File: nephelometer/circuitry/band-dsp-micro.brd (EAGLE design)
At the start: 88 x 54 mm, 41 parts, among them IC8 7805TV, J1 J5MM, T1 2N2222, T2 2N2222, U4 MotA

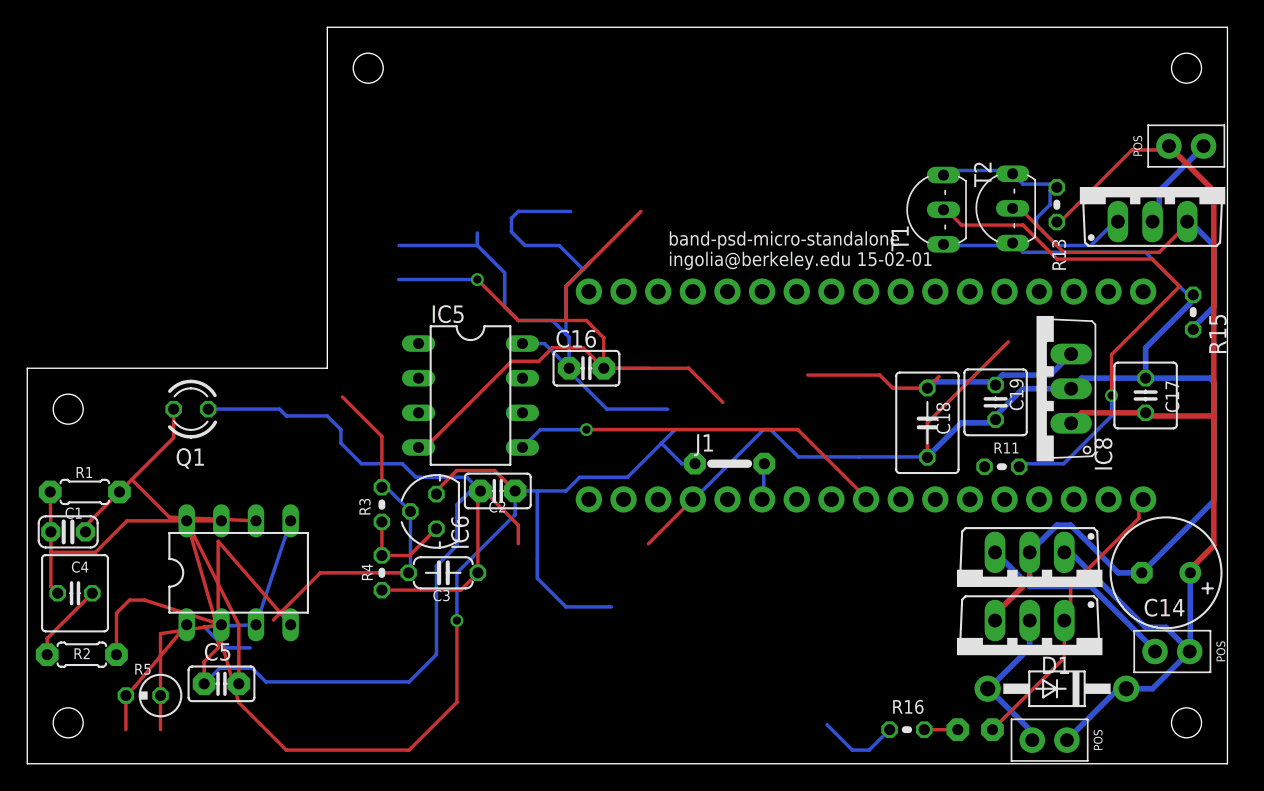
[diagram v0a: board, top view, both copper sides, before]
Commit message: Finalized minimal turbidostat circuit with Arduino Micro control
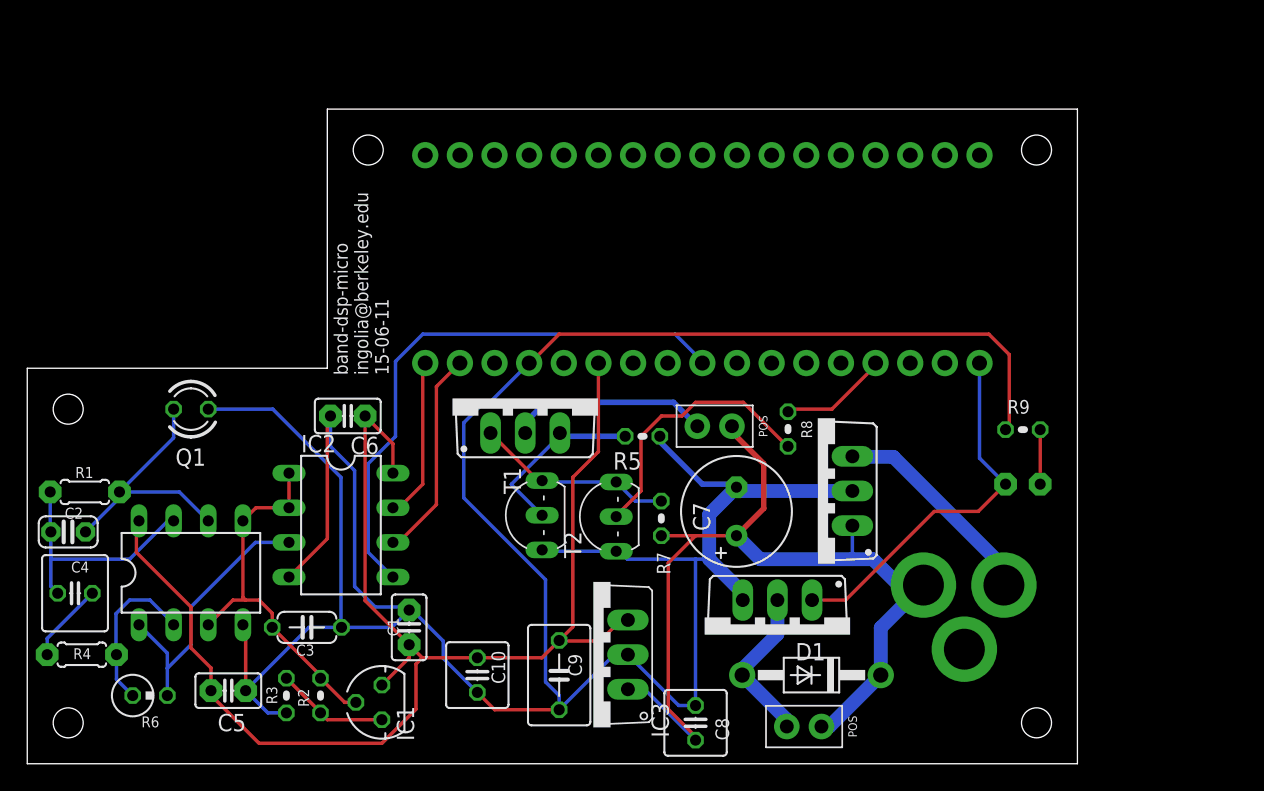
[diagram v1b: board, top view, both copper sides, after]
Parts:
- removed C14: 220µF, adafruit:E3,5-8
- removed C16: 100n, adafruit:C025-025X050
- removed C17, C19: 0.33µ, adafruit:C025-050X050
- removed C18: 22µ, adafruit:C050-045X075
- removed IC5: (no value), ingolia:DIL08
- removed IC6: (no value), v-reg:317L
- removed IC8: 7805TV, linear:TO220V
- removed R11, R13: 4K7, adafruit:0204V
- removed R15: 6.2R, adafruit:0204V
- removed R16: 330, adafruit:0204V
- removed U4: MotA, ingolia:1X02_SCREW
- added C10, C8: 0.33µ, adafruit:C025-050X050
- added C6: 100n, adafruit:C025-025X050
- added C7: 220µF, adafruit:E3,5-8
- added C9: 22µ, adafruit:C050-045X075
- added IC2, U1: (no value), ingolia:DIL08
- added IC3: 7805TV, linear:TO220V
- added R6: 2M0, adafruit:0309V
- added R7, R8: 4K7, adafruit:0204V
- added R9: 330, adafruit:0204V
- C1: value 2.2nF -> 100nF; device adafruit:C025-024X044 -> adafruit:C025-025X050
- C2: value 100nF -> 2.2nF; device adafruit:C025-025X050 -> adafruit:C025-024X044
- IC1: device ingolia:DIL08 -> v-reg:317L
- J1: value J5MM -> 2.1MMJACKTHM; device jumper:05 -> adafruit:PJ-102A
- R2: value 1K0 -> 120; device adafruit:0204/5 -> adafruit:0204V
- R4: value 120 -> 10K; device adafruit:0204V -> adafruit:0204/5
- R5: value 330K -> 10R; device adafruit:0309V -> adafruit:0204V
- U2: value (none) -> MotA
- moved Q2 48.5 mm to (36.5, 30.2)
- moved R5 41.3 mm to (45.1, 30.0)
- moved T1 37.0 mm to (36.5, 24.2)
- moved T2 36.8 mm to (41.9, 24.1)
- moved JP1 34.6 mm to (52.9, 32.0), turned to 180 degrees
- moved C2 31.6 mm to (3.00, 23.0), turned to 180 degrees
- moved U2 27.6 mm to (59.5, 10.0)
- moved C1 26.0 mm to (28.0, 16.0), turned to 270 degrees
- moved J1 25.2 mm to (75.0, 19.0), flipped to the bottom, turned to 90 degrees
- moved R4 22.8 mm to (4.00, 14.0), turned to 0 degrees
- moved Q3 18.8 mm to (55.0, 18.0)
- moved LED1 18.3 mm to (73.0, 26.5), turned to 180 degrees
- moved D1 18.0 mm to (57.5, 12.5)
- moved R2 17.8 mm to (21.5, 11.0), turned to 270 degrees
- moved Q4 16.1 mm to (60.5, 26.0), turned to 90 degrees
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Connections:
- removed net CS_ADC: IC5.5, U3.P$11
- removed net N$46: J1.2, U3.P$23
- new net N$7: IC2.5, U3.P$26
- net +12V: now also C7.+, C8.1, IC3.1, J1.TIP, Q4.G, R7.2; no longer C14.+, C17.1, IC8.1, Q3.G, R13.2, U4.1/POS
- net +5V: now also C1.2, C10.1, C6.1, C9.1, IC1.3, IC2.8, IC3.3, U1.8, U3.P$23; no longer C16.1, C18.1, C19.1, C2.2, IC1.8, IC5.8, IC6.3, IC8.3, J1.1
- net 2.5V: now also IC1.2, IC2.1, IC2.2, R2.1, U1.3, U1.5; no longer IC1.3, IC1.5, IC5.1, IC5.2, IC6.2, R3.1
- net GND: now also C1.1, C10.2, C6.2, C7.-, C8.2, C9.2, IC2.4, IC3.2, Q3.S, Q4.D, R3.1, R5.1, R9.1, U1.4; no longer C14.-, C16.2, C17.2, C18.2, C19.2, C2.1, IC1.4, IC5.4, IC8.2, Q3.D, Q4.S, R15.1, R16.1, R4.1
- net LEDCTRL: now also R8.2, T2.B; no longer R11.2, T1.B
- net N$1: now also C2.1, U1.6; no longer C1.1, IC1.6
- net N$14: now also R5.2, T1.B; no longer R15.2, T2.B
- net N$16: now also R9.2; no longer R16.2
- net N$19: now also Q3.G; no longer Q4.G
- net N$2: now also R4.1; no longer R2.1
- net N$22: now also C2.2, U1.7; no longer C1.2, IC1.7
- net N$25: now also R4.2, R6.1, U1.2; no longer IC1.2, R2.2, R5.1
- net N$26: now also IC2.3, R6.2, U1.1; no longer IC1.1, IC5.3, R5.2
- net N$3: now also Q3.D, U2.2; no longer Q4.D, U4.2
- net N$35: now also IC1.1, R2.2; no longer IC6.1, R4.2
- net N$4: now also IC2.6; no longer IC5.6
- net N$47: now also J1.RING, Q4.S; no longer Q3.S, U2.2
- net N$5: now also R8.1, U3.P$31; no longer R11.1, U3.P$1
- net N$6: now also IC2.7; no longer IC5.7
- net N$8: now also R7.1; no longer R13.1
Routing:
- net +5V: track 172.6 -> 102.7 mm, vias 1 -> 0
- net GND: track 279.5 -> 227.2 mm, vias 1 -> 0
- net N$7: track 0.00 -> 41.7 mm
- net CS_ADC: track 27.8 -> 0.00 mm, vias 1 -> 0
- net LEDCTRL: track 39.8 -> 19.8 mm, vias 1 -> 0
- net N$4: track 0.00 -> 15.4 mm
- net 2.5V: track 43.0 -> 27.6 mm
- net +12V: track 84.8 -> 70.0 mm
- net N$6: track 0.00 -> 11.9 mm
- net N$14: track 24.5 -> 13.3 mm
- net N$26: track 9.35 -> 20.4 mm
- net N$25: track 23.0 -> 12.0 mm
- net N$5: track 0.00 -> 8.00 mm
- net N$18: track 7.18 -> 14.7 mm
- net N$19: track 21.2 -> 27.4 mm
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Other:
- board size 88 x 54 mm -> 77 x 48 mm
- board text added: "band-dsp-micro ingolia@berkeley.edu 15-06-11"
- board text removed: "band-psd-micro-standalone ingolia@berkeley.edu 15-02-01"
